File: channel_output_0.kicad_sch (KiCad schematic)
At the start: 35 parts, among them IC7 TPS56637RPAR, J12 Conn_01x02, Q7 2N7002_SOT-23-3, U5 MCP4725xxx-xCH

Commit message: Update footprint for testpoints
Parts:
- TP1, TP13, TP17, TP19, TP22, TP26, TP5, TP9: footprint Hardware Components Footprints:TP_2.54mm_THT_Keystone_500x -> TestPoint:TestPoint_Pad_1.5x1.5mm

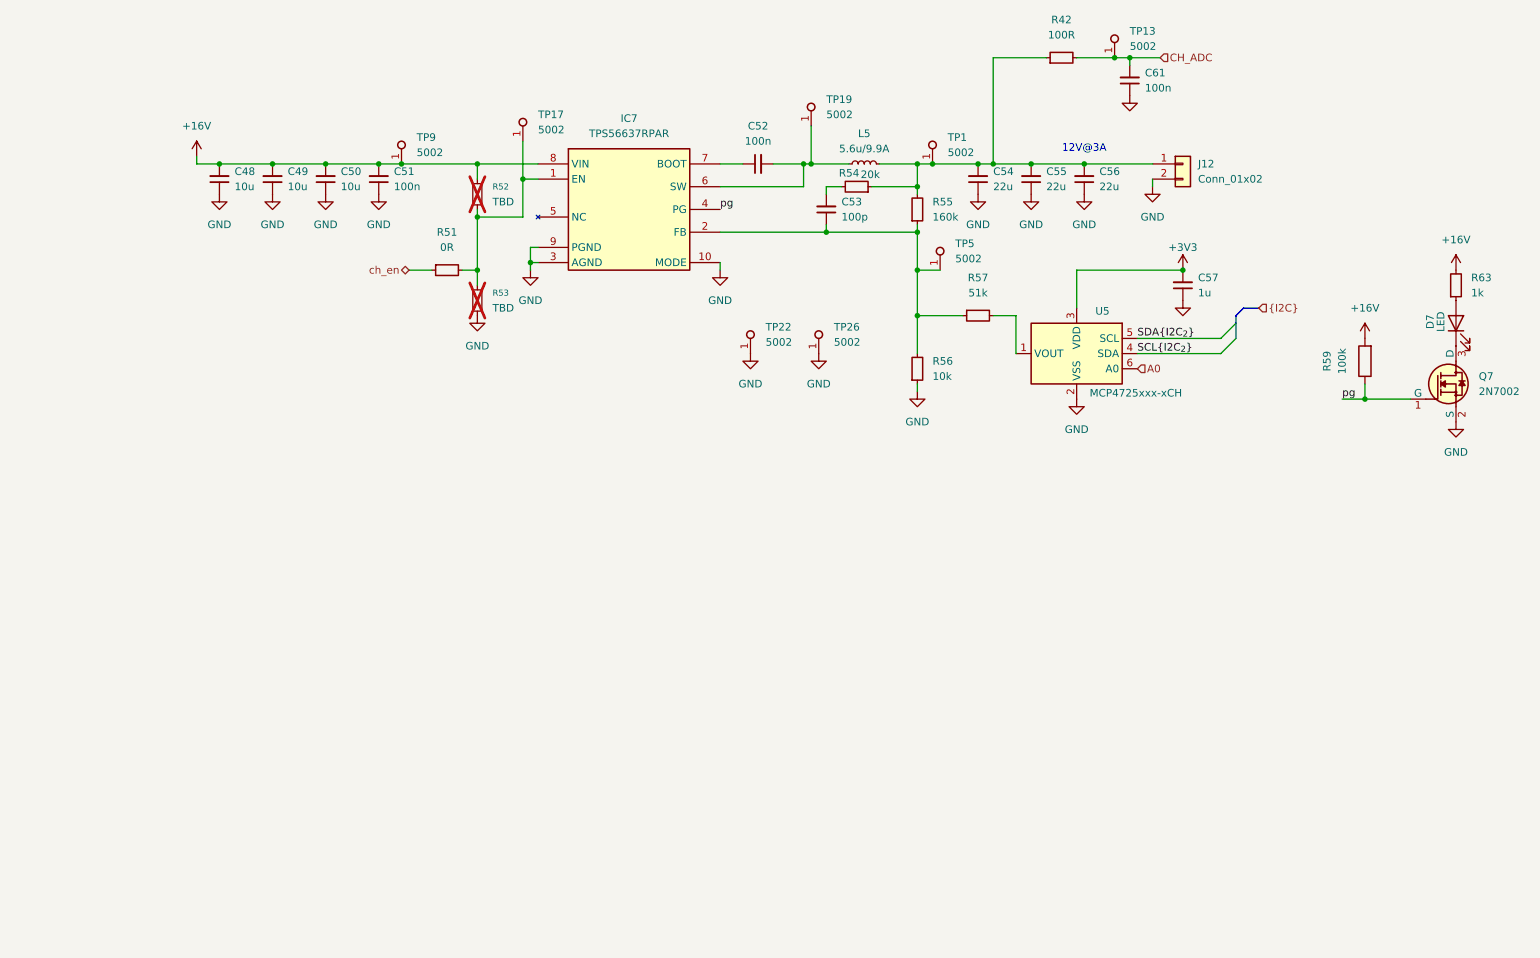
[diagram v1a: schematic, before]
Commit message: Remove redundant resistors
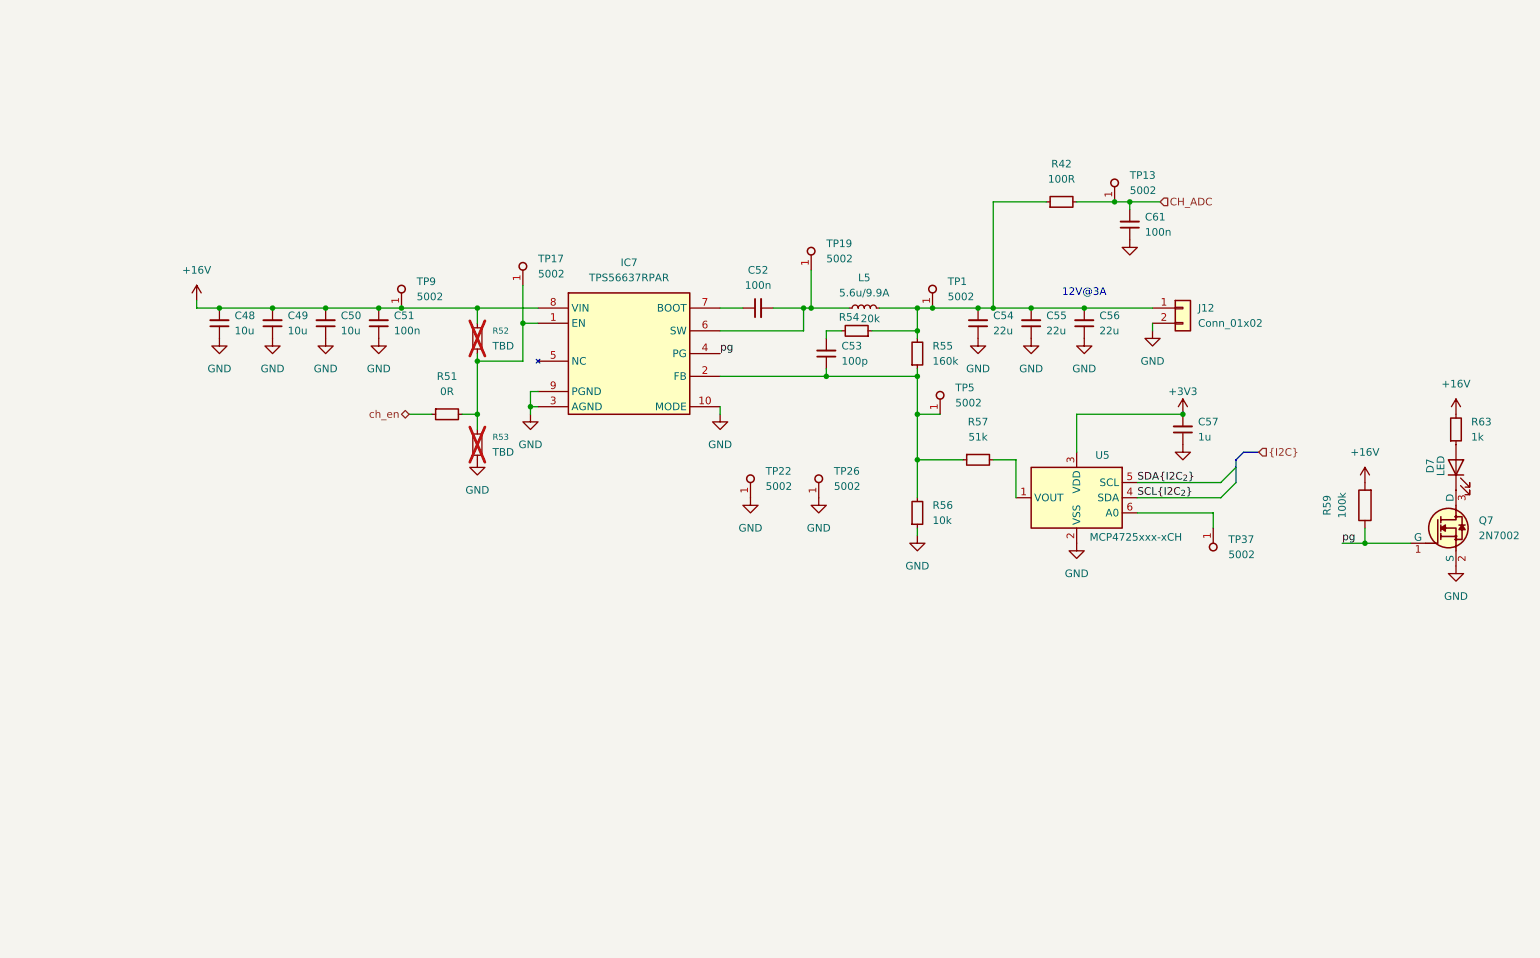
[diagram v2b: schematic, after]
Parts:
- added TP37: TP_2.54mm_THT_5002, TestPoint:TestPoint_Pad_1.5x1.5mm, symbol Hardware Components:TP_2.54mm_THT_5002
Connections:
- net A0: no longer names the net of U5.6 (A0)
- net A0: now also TP37.1
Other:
- moved on the sheet: C48, C49, C50, C51, C52, C53, C54, C55, C56, C57, C61, D7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

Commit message: Added new DC/DC converter design
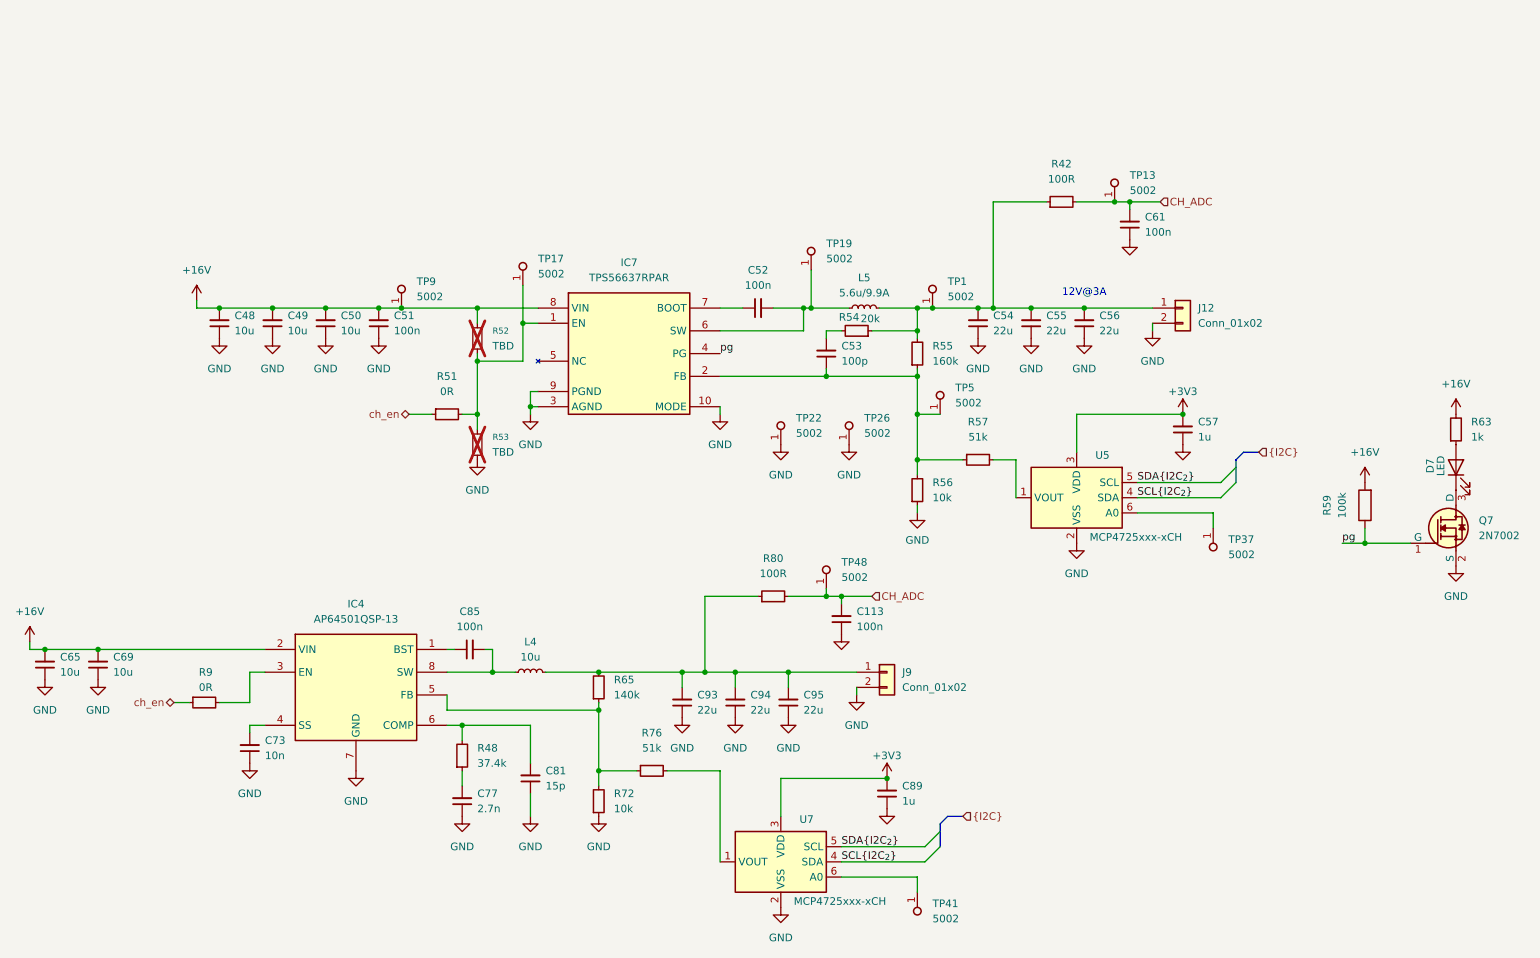
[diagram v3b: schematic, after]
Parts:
- added C113: C_100n_50V_X8L_0402, Hardware Components Footprints:C_0402_1005Metric, symbol lib:C_100n_50V_X8L_0402
- added C65, C69, C73, C77, C81: C_10u_1206, Hardware Components Footprints:C_1206_3216Metric, symbol Hardware Components:C_10u_1206
- added C85: C_100n_16V_X7R_0402, Hardware Components Footprints:C_0402_1005Metric, symbol Hardware Components:C_100n_16V_X7R_0402
- added C89: C_1u_0402, Hardware Components Footprints:C_0402_1005Metric, symbol lib:C_1u_0402
- added C93, C94, C95: C_22u_25V_X7R_1210, Hardware Components Footprints:C_1210_3225Metric, symbol Hardware Components:C_22u_25V_X7R_1210
- added IC4: AP64501QSP-13, SOIC127P600X163-9N, symbol ap3:AP64501QSP-13
- added J9: Conn_01x02, TerminalBlock_Phoenix:TerminalBlock_Phoenix_MKDS-1,5-2-5.08_1x02_P5.08mm_Horizontal, symbol lib:Conn_01x02
- added L4: L_4u7_11A_Coilcraft-XAL6060, Hardware Components Footprints:L_Coilcraft-XAL6060, symbol Hardware Components:L_4u7_11A_Coilcraft-XAL6060
- added R48, R65, R72: R_160k_0402, Hardware Components Footprints:R_0402_1005Metric, symbol Hardware Components:R_160k_0402
- added R76: R_51k_0402, Hardware Components Footprints:R_0402_1005Metric, symbol Hardware Components:R_51k_0402
- added R80: R_100R_0402, Hardware Components Footprints:R_0402_1005Metric, symbol lib:R_100R_0402
- added R9: R_0R_0402, Hardware Components Footprints:R_0402_1005Metric, symbol lib:R_0R_0402
- added TP41, TP48: TP_2.54mm_THT_5002, TestPoint:TestPoint_Pad_1.5x1.5mm, symbol Hardware Components:TP_2.54mm_THT_5002
- added U7: MCP4725xxx-xCH, Package_TO_SOT_SMD:SOT-23-6, symbol Analog_DAC:MCP4725xxx-xCH
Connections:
- net +16V: now also C65.2, C69.2, IC4.2 (VIN)
- net +3V3: now also C89.2, U7.3 (VDD)
- net CH_ADC: now also C113.2, R80.2, TP48.1
- net GND: now also C113.1, C65.1, C69.1, C73.1, C77.1, C81.1, C89.1, C93.1, C94.1, C95.1, IC4.7 (GND), J9.2 (Pin_2), R72.1, U7.2 (VSS)
- net SCL{I2C_{2}}: now also U7.4 (SDA)
- net SDA{I2C_{2}}: now also U7.5 (SCL)
- net ch_en: now also R9.1
- new net: IC4.5 (FB), R65.1, R72.2, R76.1
- new net: C93.2, C94.2, C95.2, J9.1 (Pin_1), L4.2, R65.2, R80.1
- new net: C77.2, R48.1
- new net: C81.2, IC4.6 (COMP), R48.2
- new net: R76.2, U7.1 (VOUT)
- new net: TP41.1, U7.6 (A0)
- new net: C73.2, IC4.4 (SS)
- new net: C85.1, IC4.1 (BST)
- new net: C85.2, IC4.8 (SW), L4.1
- new net: IC4.3 (EN), R9.2
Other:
- moved on the sheet: R56, TP22, TP26

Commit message: Add lead compensator, move leds to uC, redo resistors
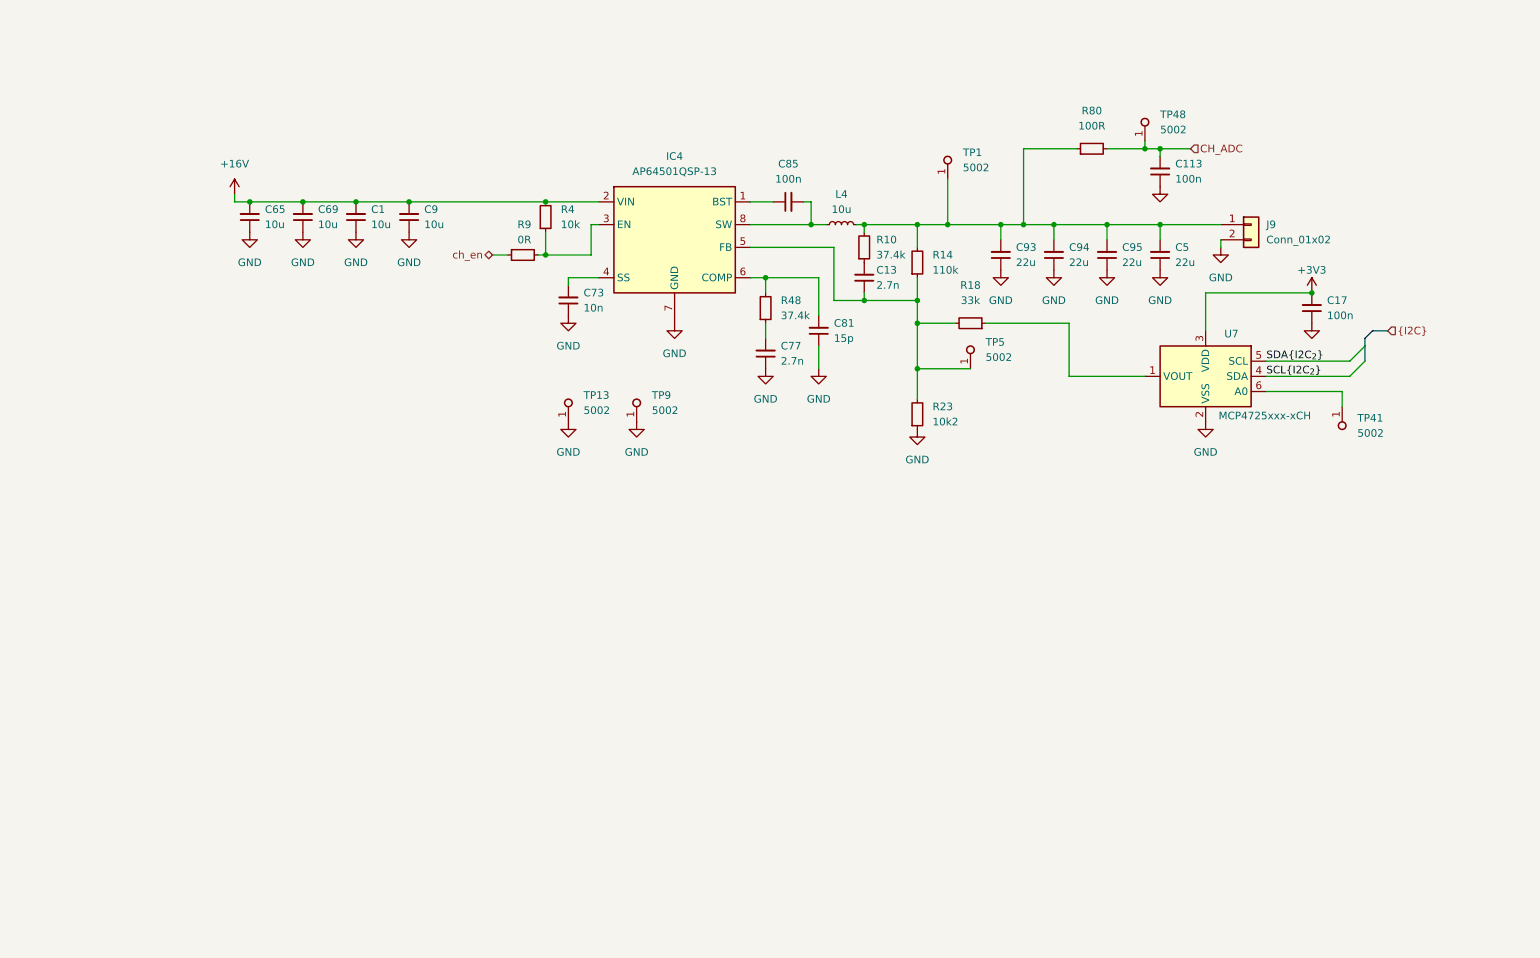
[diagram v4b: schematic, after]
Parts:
- removed C48, C49, C50: C_10u_1206, Hardware Components Footprints:C_1206_3216Metric, symbol Hardware Components:C_10u_1206
- removed C51, C52: C_100n_16V_X7R_0402, Hardware Components Footprints:C_0402_1005Metric, symbol Hardware Components:C_100n_16V_X7R_0402
- removed C53: C_100p_0402, Hardware Components Footprints:C_0402_1005Metric, symbol Hardware Components:C_100p_0402
- removed C54, C55, C56: C_22u_25V_X7R_1210, Hardware Components Footprints:C_1210_3225Metric, symbol Hardware Components:C_22u_25V_X7R_1210
- removed C57, C89: C_1u_0402, Hardware Components Footprints:C_0402_1005Metric, symbol lib:C_1u_0402
- removed C61: C_100n_50V_X8L_0402, Hardware Components Footprints:C_0402_1005Metric, symbol lib:C_100n_50V_X8L_0402
- removed D7: LED, LED_SMD:LED_0603_1608Metric, symbol lib:LED
- removed IC7: TPS56637RPAR, Package_DFN_QFN:Texas_RPU0010A_VQFN-HR-10_2x2mm_P0.5mm, symbol lib:TPS56637RPAR_1
- removed J12: Conn_01x02, TerminalBlock_Phoenix:TerminalBlock_Phoenix_MKDS-1,5-2-5.08_1x02_P5.08mm_Horizontal, symbol lib:Conn_01x02
- removed L5: L_4u7_11A_Coilcraft-XAL6060, Hardware Components Footprints:L_Coilcraft-XAL6060, symbol Hardware Components:L_4u7_11A_Coilcraft-XAL6060
- removed Q7: 2N7002_SOT-23-3, Hardware Components Footprints:SOT-23-3, symbol lib:2N7002_SOT-23-3
- removed R42: R_100R_0402, Hardware Components Footprints:R_0402_1005Metric, symbol lib:R_100R_0402
- removed R51: R_0R_0402, Hardware Components Footprints:R_0402_1005Metric, symbol lib:R_0R_0402
- removed R52, R53: TBD, Hardware Components Footprints:R_0402_1005Metric, symbol lib:R_Small
- removed R54: R_20k_0402, Hardware Components Footprints:R_0402_1005Metric, symbol Hardware Components:R_20k_0402
- removed R55, R65, R72: R_160k_0402, Hardware Components Footprints:R_0402_1005Metric, symbol Hardware Components:R_160k_0402
- removed R56: R_10k_0402, Hardware Components Footprints:R_0402_1005Metric, symbol lib:R_10k_0402
- removed R57, R76: R_51k_0402, Hardware Components Footprints:R_0402_1005Metric, symbol Hardware Components:R_51k_0402
- removed R59: 100k, Hardware Components Footprints:R_0402_1005Metric, symbol lib:R
- removed R63: R_1k_0402, Hardware Components Footprints:R_0402_1005Metric, symbol Hardware Components:R_1k_0402
- removed TP17, TP19, TP22, TP26, TP37: TP_2.54mm_THT_5002, TestPoint:TestPoint_Pad_1.5x1.5mm, symbol Hardware Components:TP_2.54mm_THT_5002
- removed U5: MCP4725xxx-xCH, Package_TO_SOT_SMD:SOT-23-6, symbol Analog_DAC:MCP4725xxx-xCH
- added C1, C13, C9: C_10u_1206, Hardware Components Footprints:C_1206_3216Metric, symbol Hardware Components:C_10u_1206
- added C17: C_100n_16V_X7R_0402, Hardware Components Footprints:C_0402_1005Metric, symbol Hardware Components:C_100n_16V_X7R_0402
- added C5: C_22u_25V_X7R_1210, Hardware Components Footprints:C_1210_3225Metric, symbol Hardware Components:C_22u_25V_X7R_1210
- added R10, R4: R_160k_0402, Hardware Components Footprints:R_0402_1005Metric, symbol Hardware Components:R_160k_0402
- added R14: R_110k_0402, Hardware Components Footprints:R_0402_1005Metric, symbol Hardware Components:R_110k_0402
- added R18: R_33k_0402, Hardware Components Footprints:R_0402_1005Metric, symbol Hardware Components:R_33k_0402
- added R23: R_10k2_0402, Hardware Components Footprints:R_0402_1005Metric, symbol Hardware Components:R_10k2_0402
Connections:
- net +16V: now also C1.2, C9.2, R4.2; no longer TP9.1
- net +3V3: now also C17.2
- net CH_ADC: no longer TP13.1
- net GND: now also TP13.1, TP9.1, C1.1, C17.1, C5.1, C9.1, R23.1
- net at IC4.5 (FB): now also TP5.1, C13.1, R14.1, R18.2, R23.2
- net at C93.2, C94.2, C95.2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: now also TP1.1, C5.2, R10.2, R14.2
- net at U7.1 (VOUT): now also R18.1
- net at IC4.3 (EN), R9.2: now also R4.1
- new net: C13.2, R10.1
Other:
- note removed: "12V@3A"
- moved on the sheet: C113, C65, C69, C73, C77, C81, C85, C93, C94, C95, IC4, J9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

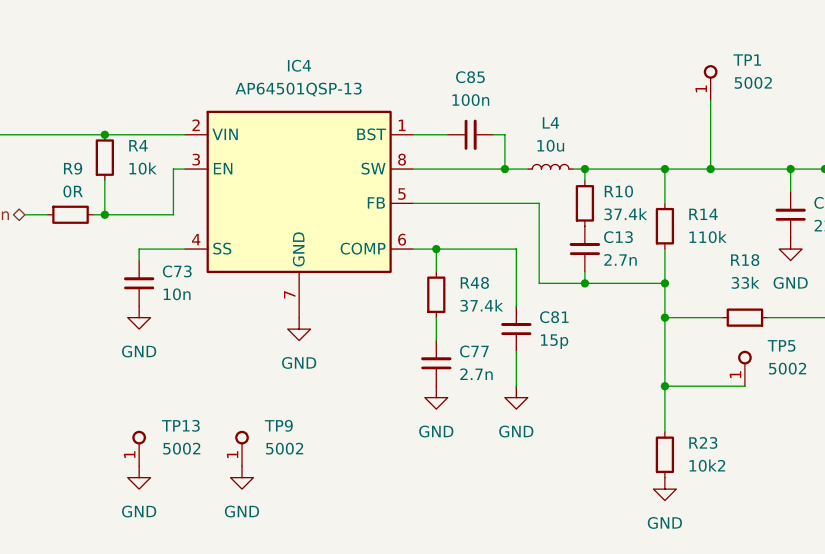
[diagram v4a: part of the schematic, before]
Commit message: update inductor
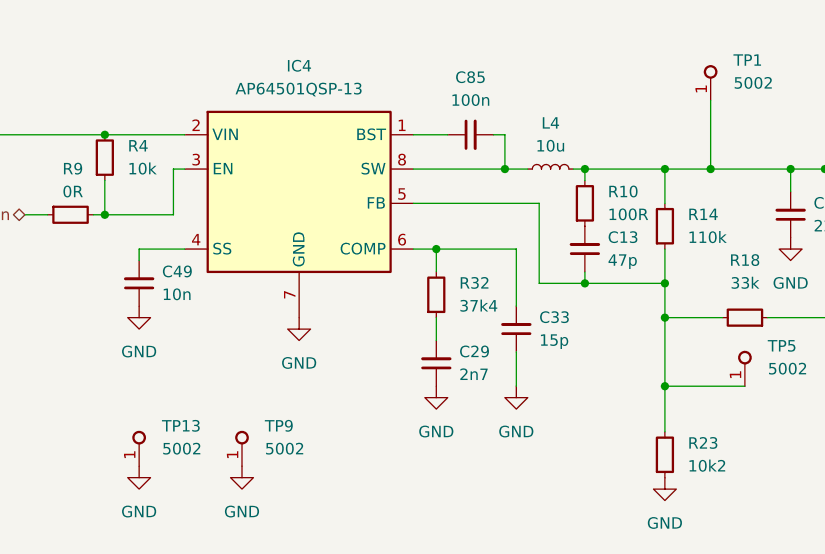
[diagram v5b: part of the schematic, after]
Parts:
- removed C13, C73, C77, C81: C_10u_1206, Hardware Components Footprints:C_1206_3216Metric, symbol Hardware Components:C_10u_1206
- removed R10, R4, R48: R_160k_0402, Hardware Components Footprints:R_0402_1005Metric, symbol Hardware Components:R_160k_0402
- added C13: C_47p_0402, Hardware Components Footprints:C_0402_1005Metric, symbol Hardware Components:C_47p_0402
- added C29: C_2n7_0603, Hardware Components Footprints:C_0603_1608Metric, symbol Hardware Components:C_2n7_0603
- added C33: C_15p_0402, Hardware Components Footprints:C_0402_1005Metric, symbol Hardware Components:C_15p_0402
- added C49: C_10n_25V_X8L_0402, Hardware Components Footprints:C_0402_1005Metric, symbol Hardware Components:C_10n_25V_X8L_0402
- added R10: R_100R_0402, Hardware Components Footprints:R_0402_1005Metric, symbol lib:R_100R_0402
- added R32: R_37k4_0402, Hardware Components Footprints:R_0402_1005Metric, symbol Hardware Components:R_37k4_0402
- added R4: R_10k_0402, Hardware Components Footprints:R_0402_1005Metric, symbol Hardware Components:R_10k_0402
- L4: value L_4u7_11A_Coilcraft-XAL6060 -> L_10u_6.5A; footprint Hardware Components Footprints:L_Coilcraft-XAL6060 -> Inductor_SMD:L_Bourns_SRR1210A; Author Antmicro -> (none); IMax 9.9A -> (none); ISat 9A -> 6.5A; License Apache-2.0 -> (none); MPN XAL6060-562MEB -> SRR1210A-100M; Size 6.36x6.56 -> (none)
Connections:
- net +16V: now also R4.2
- net GND: now also C29.1, C33.1, C49.1
- net at C5.2, C93.2, C94.2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: now also R10.2
- net at IC4.6 (COMP): now also C33.2, R32.2
- net at IC4.5 (FB), R14.1, R18.2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: now also C13.1
- net at IC4.3 (EN), R9.2: now also R4.1
- net at IC4.4 (SS): now also C49.2
- new net: C13.2, R10.1
- new net: C29.2, R32.1
